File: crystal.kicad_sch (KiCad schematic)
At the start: 4 parts, among them Y1 Crystal_GND24

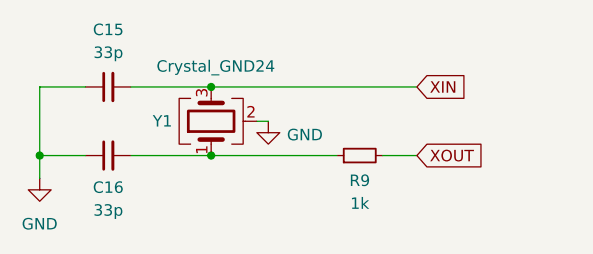
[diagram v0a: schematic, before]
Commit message: 4 layers
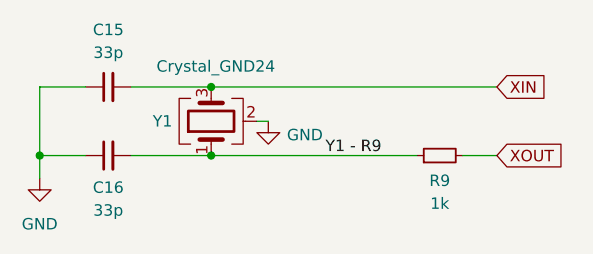
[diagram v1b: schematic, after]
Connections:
- net Y1 - R9: now reaches C16.2, R9.1, Y1.1
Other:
- moved on the sheet: R9
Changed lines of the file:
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@@
 	(wire
 		(pts
-			(xy 146.05 102.87) (xy 160.02 102.87)
+			(xy 146.05 95.25) (xy 177.8 95.25)
 		)
 		(stroke
@@
 	(wire
 		(pts
-			(xy 165.1 102.87) (xy 168.91 102.87)
+			(xy 173.99 102.87) (xy 177.8 102.87)
 		)
 		(stroke
@@
 	(wire
 		(pts
-			(xy 146.05 95.25) (xy 168.91 95.25)
+			(xy 146.05 102.87) (xy 168.91 102.87)
 		)
 		(stroke
@@
 			(width 0)
 			(type default)
+		)
+	)
+	(label "Y1 - R9"
+		(at 158.75 102.87 0)
+		(effects
+			(font
+				(size 1.27 1.27)
+			)
+			(justify left bottom)
 		)
 	)
 	(global_label "XOUT"
 		(shape input)
-		(at 168.91 102.87 0)
+		(at 177.8 102.87 0)
 		(fields_autoplaced yes)
 		(effects
@@
 		)
 		(property "Intersheetrefs" "${INTERSHEET_REFS}"
-			(at 176.7333 102.87 0)
+			(at 185.6233 102.87 0)
 			(effects
 				(font
@@
 	(global_label "XIN"
 		(shape input)
-		(at 168.91 95.25 0)
+		(at 177.8 95.25 0)
 		(fields_autoplaced yes)
 		(effects
@@
 		)
 		(property "Intersheetrefs" "${INTERSHEET_REFS}"
-			(at 175.04 95.25 0)
+			(at 183.93 95.25 0)
 			(effects
 				(font
@@
 	(symbol
 		(lib_id "Device:R_Small")
-		(at 162.56 102.87 90)
+		(at 171.45 102.87 90)
 		(unit 1)
 		(exclude_from_sim no)
@@
 		(dnp no)
 		(property "Reference" "R9"
-			(at 162.56 105.664 90)
+			(at 171.45 105.664 90)
 			(effects
 				(font
@@
 		)
 		(property "Value" "1k"
-			(at 162.56 108.204 90)
+			(at 171.45 108.204 90)
 			(effects
 				(font
@@
 		)
 		(property "Footprint" "Library:R_0402_1005Metric"
-			(at 162.56 102.87 0)
+			(at 171.45 102.87 0)
 			(effects
 				(font
@@
 		)
 		(property "Datasheet" "~"
-			(at 162.56 102.87 0)
+			(at 171.45 102.87 0)
 			(effects
 				(font
@@
 		)
 		(property "Description" "Resistor, small symbol"
-			(at 162.56 102.87 0)
-			(effects
-				(font
+			(at 171.45 102.87 0)
+			(effects
+				(font

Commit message: BOM
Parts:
- C15, C16: LCSC (none) -> C1562
- R9: LCSC (none) -> C11702
- Y1: LCSC (none) -> C20625731
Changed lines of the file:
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@@
 			)
 		)
-		(property "Datasheet" "~"
+		(property "Datasheet" "kicad-embed://C1562.pdf"
 			(at 134.62 102.87 0)
 			(effects
@@
 		(property "Description" "Unpolarized capacitor, small symbol"
 			(at 134.62 102.87 0)
+			(effects
+				(font
+					(size 1.27 1.27)
+				)
+				(hide yes)
+			)
+		)
+		(property "LCSC" "C1562"
+			(at 134.62 102.87 90)
+			(effects
+				(font
+					(size 1.27 1.27)
+				)
+				(hide yes)
+			)
+		)
+		(property "KLC_S3.3" ""
+			(at 134.62 102.87 90)
+			(effects
+				(font
+					(size 1.27 1.27)
+				)
+				(hide yes)
+			)
+		)
+		(property "KLC_S4.1" ""
+			(at 134.62 102.87 90)
+			(effects
+				(font
+					(size 1.27 1.27)
+				)
+				(hide yes)
+			)
+		)
+		(property "KLC_S4.2_DVDD" ""
+			(at 134.62 102.87 90)
+			(effects
+				(font
+					(size 1.27 1.27)
+				)
+				(hide yes)
+			)
+		)
+		(property "KLC_S4.2_VREG_VOUT" ""
+			(at 134.62 102.87 90)
 			(effects
 				(font
@@
 			)
 		)
-		(property "Datasheet" "~"
+		(property "Datasheet" "kicad-embed://C11702.pdf"
 			(at 171.45 102.87 0)
 			(effects
@@
 		(property "Description" "Resistor, small symbol"
 			(at 171.45 102.87 0)
+			(effects
+				(font
+					(size 1.27 1.27)
+				)
+				(hide yes)
+			)
+		)
+		(property "LCSC" "C11702"
+			(at 171.45 102.87 90)
+			(effects
+				(font
+					(size 1.27 1.27)
+				)
+				(hide yes)
+			)
+		)
+		(property "KLC_S3.3" ""
+			(at 171.45 102.87 90)
+			(effects
+				(font
+					(size 1.27 1.27)
+				)
+				(hide yes)
+			)
+		)
+		(property "KLC_S4.1" ""
+			(at 171.45 102.87 90)
+			(effects
+				(font
+					(size 1.27 1.27)
+				)
+				(hide yes)
+			)
+		)
+		(property "KLC_S4.2_DVDD" ""
+			(at 171.45 102.87 90)
+			(effects
+				(font
+					(size 1.27 1.27)
+				)
+				(hide yes)
+			)
+		)
+		(property "KLC_S4.2_VREG_VOUT" ""
+			(at 171.45 102.87 90)
 			(effects
 				(font
@@
 			)
 		)
-		(property "Datasheet" "kicad-embed://C9002_crystal.pdf"
+		(property "Datasheet" "kicad-embed://C20625731.pdf"
 			(at 146.05 99.06 0)
 			(effects
@@
 			(at 161.29 99.06 0)
 			(show_name yes)
+			(effects
+				(font
+					(size 1.27 1.27)
+				)
+				(hide yes)
+			)
+		)
+		(property "LCSC" "C20625731"
+			(at 146.05 99.06 90)
+			(effects
+				(font
+					(size 1.27 1.27)
+				)
+				(hide yes)
+			)
+		)
+		(property "KLC_S4.2_DVDD" ""
+			(at 146.05 99.06 90)
+			(effects
+				(font
+					(size 1.27 1.27)
+				)
+				(hide yes)
+			)
+		)
+		(property "KLC_S4.2_VREG_VOUT" ""
+			(at 146.05 99.06 90)
 			(effects
 				(font
@@
 			)
 		)
-		(property "Datasheet" "~"
+		(property "Datasheet" "kicad-embed://C1562.pdf"
 			(at 134.62 95.25 0)
 			(effects
@@
 			(effects
 				(font
+					(size 1.27 1.27)
+				)
+				(hide yes)
+			)
+		)
+		(property "LCSC" "C1562"
+			(at 134.62 95.25 90)
+			(effects
+				(font
+					(size 1.27 1.27)
+				)
+				(hide yes)
+			)
+		)
+		(property "KLC_S3.3" ""
+			(at 134.62 95.25 90)
+			(effects
+				(font
+					(size 1.27 1.27)
+				)
+				(hide yes)
+			)
+		)
+		(property "KLC_S4.1" ""
+			(at 134.62 95.25 90)
+			(effects
+				(font
+					(size 1.27 1.27)
+				)
+				(hide yes)
+			)
+		)
+		(property "KLC_S4.2_DVDD" ""
+			(at 134.62 95.25 90)
+			(effects
+				(font
+					(size 1.27 1.27)
+				)
+				(hide yes)
+			)
+		)
+		(property "KLC_S4.2_VREG_VOUT" ""
+			(at 134.62 95.25 90)
+			(effects
+				(font
